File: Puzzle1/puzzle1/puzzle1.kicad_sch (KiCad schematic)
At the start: 1 part, among them U1 PCA9555D

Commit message: small update, nothing defined
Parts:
- removed U1: PCA9555D, Package_SO:SOIC-24W_7.5x15.4mm_P1.27mm, symbol Interface_Expansion:PCA9555D
- added J3: Raspberry_Pi_2_3, Connector_PinSocket_2.54mm:PinSocket_2x20_P2.54mm_Vertical, symbol Connector:Raspberry_Pi_2_3
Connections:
- net +5V: now also J3.2 (5V), J3.4 (5V)
- net GND: now also J3.14 (GND), J3.20 (GND), J3.25 (GND), J3.30 (GND), J3.34 (GND), J3.39 (GND), J3.6 (GND), J3.9 (GND)
- new net +3.3V: J3.1 (3V3), J3.17 (3V3)
- new net SCL: J3.5 (SCL/GPIO3)
- new net SDA: J3.3 (SDA/GPIO2)
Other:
- added sheet GPIOExpander1 (GPIOExpander.kicad_sch)
- added sheet GPIOExpander2 (GPIOExpander.kicad_sch)

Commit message: update
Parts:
- removed J3: Raspberry_Pi_2_3, Connector_PinSocket_2.54mm:PinSocket_2x20_P2.54mm_Vertical, symbol Connector:Raspberry_Pi_2_3
- added J1: Conn_01x04_Pin, Connector_JST:JST_XH_B4B-XH-A_1x04_P2.50mm_Vertical, symbol Connector:Conn_01x04_Pin
- added R1, R2: 4.7k, Resistor_SMD:R_0603_1608Metric_Pad0.98x0.95mm_HandSolder, symbol Device:R
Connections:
- net +5V: now also J1.1 (Pin_1), R1.1, R2.1
- net GND: now also J1.4 (Pin_4)
- net SCL: now also J1.2 (Pin_2), R2.2
- net SDA: now also J1.3 (Pin_3), R1.2
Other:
- removed sheet GPIOExpander2
- sheet GPIOExpander1 ports: added GND, SCL, SDA, VCC; removed none

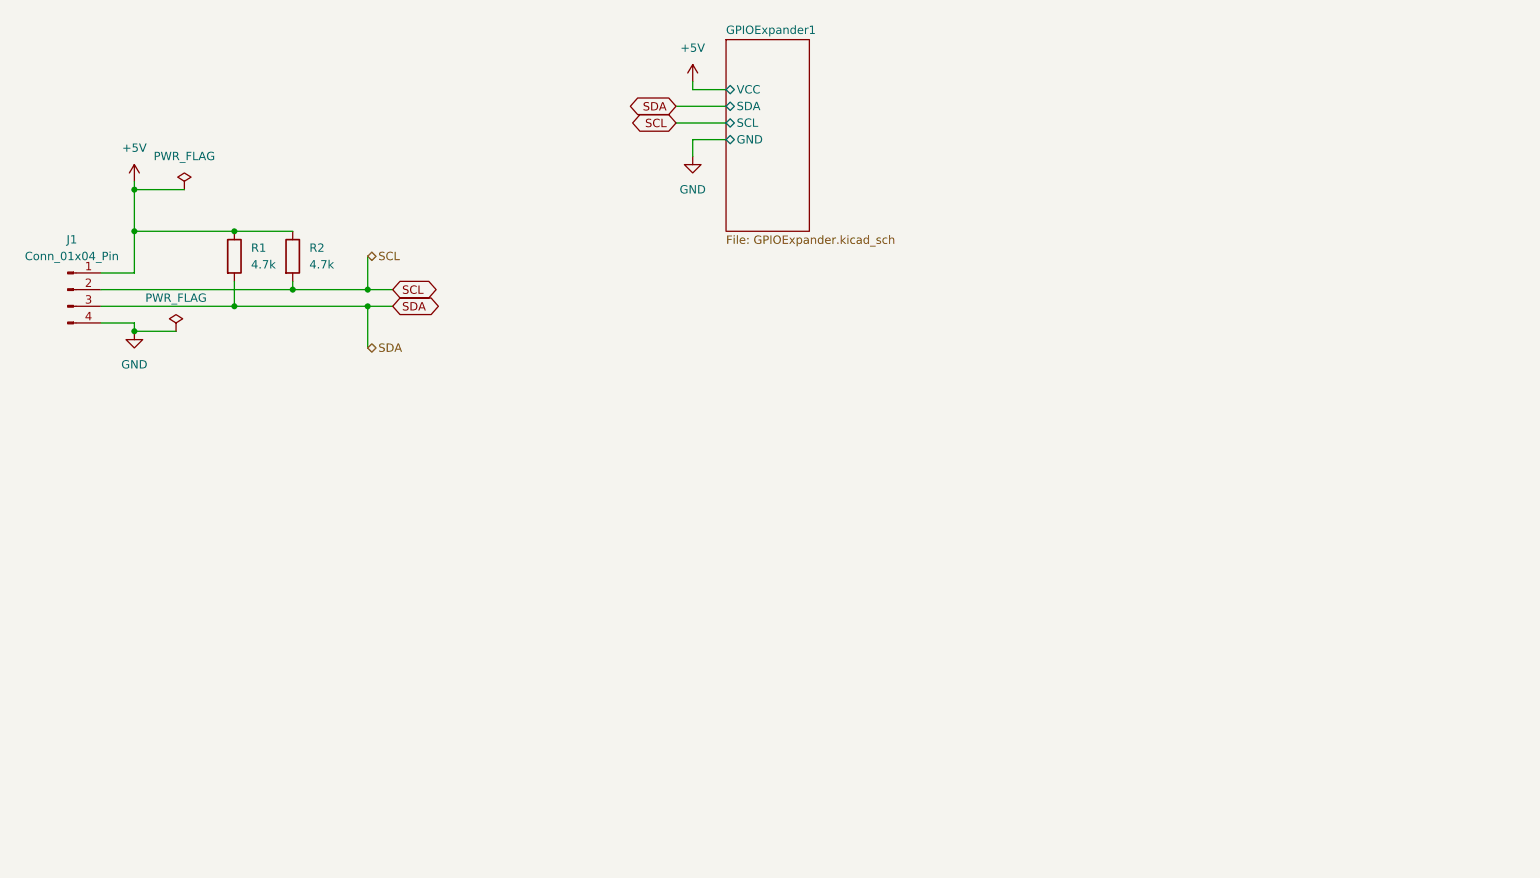
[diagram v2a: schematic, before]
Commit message: update
not finished, but working with the busses now
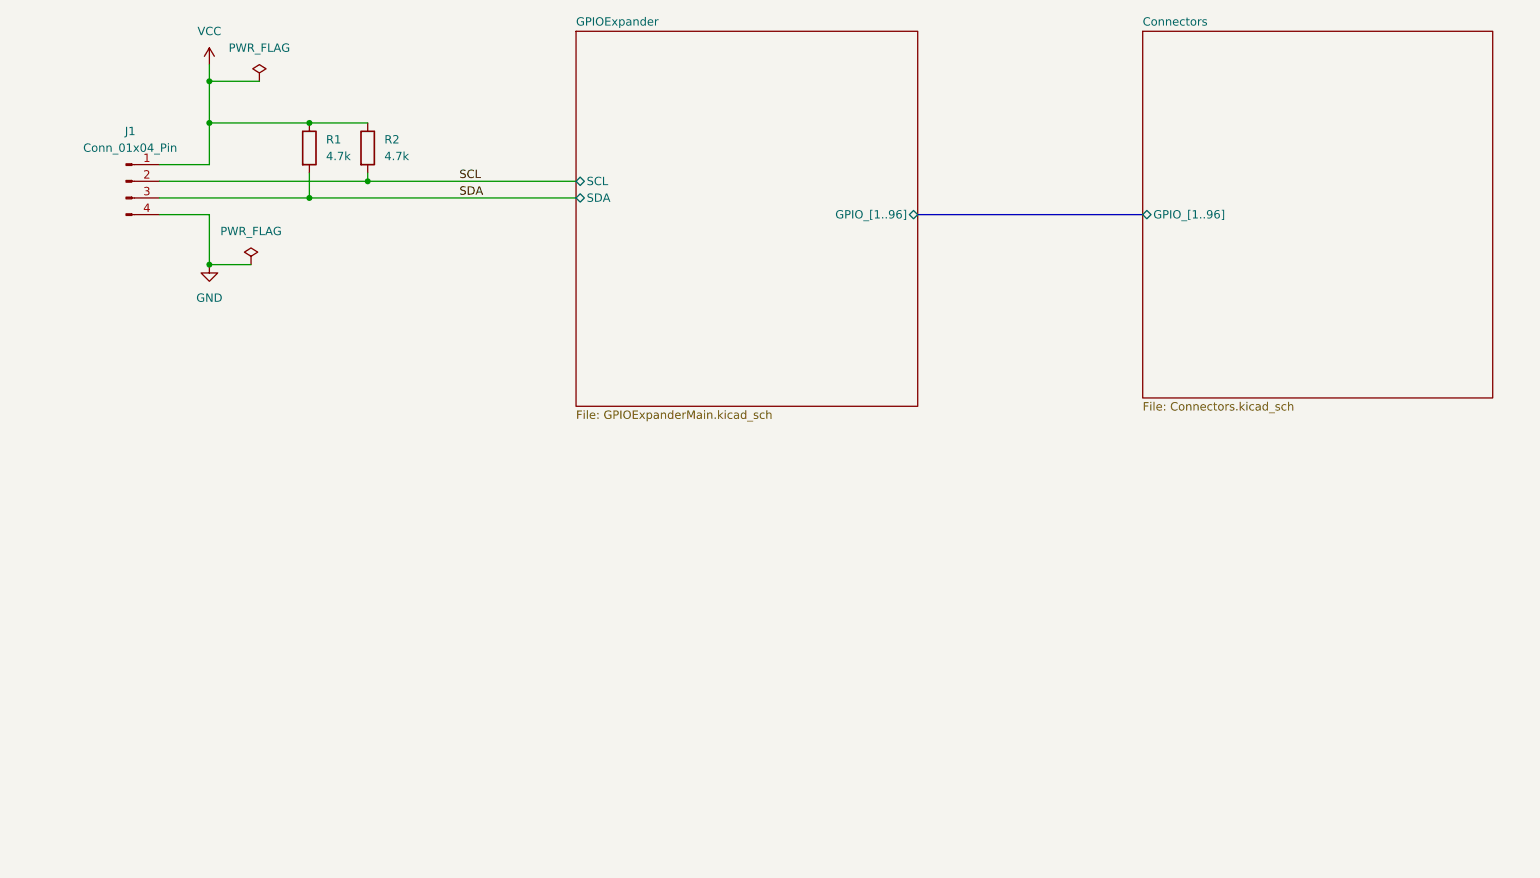
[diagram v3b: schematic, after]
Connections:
- net +5V renamed VCC
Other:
- removed sheet GPIOExpander1
- added sheet Connectors (Connectors.kicad_sch)
- added sheet GPIOExpander (GPIOExpanderMain.kicad_sch)
- moved on the sheet: R1, R2

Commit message: added base board to designs, not fully done yet
weekend update
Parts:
- added H1, H2, H3: MountingHole_Pad, MountingHole:MountingHole_3.2mm_M3_DIN965_Pad, symbol Mechanical:MountingHole_Pad
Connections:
- net GND: now also H1.1, H2.1, H3.1
